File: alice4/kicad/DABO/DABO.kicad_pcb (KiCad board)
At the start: 2 copper layers, 4 parts, among them P1 CONN_01X20, P2 CONN_01X20, P3 CONN_02X20, U1 touchscreen_controller

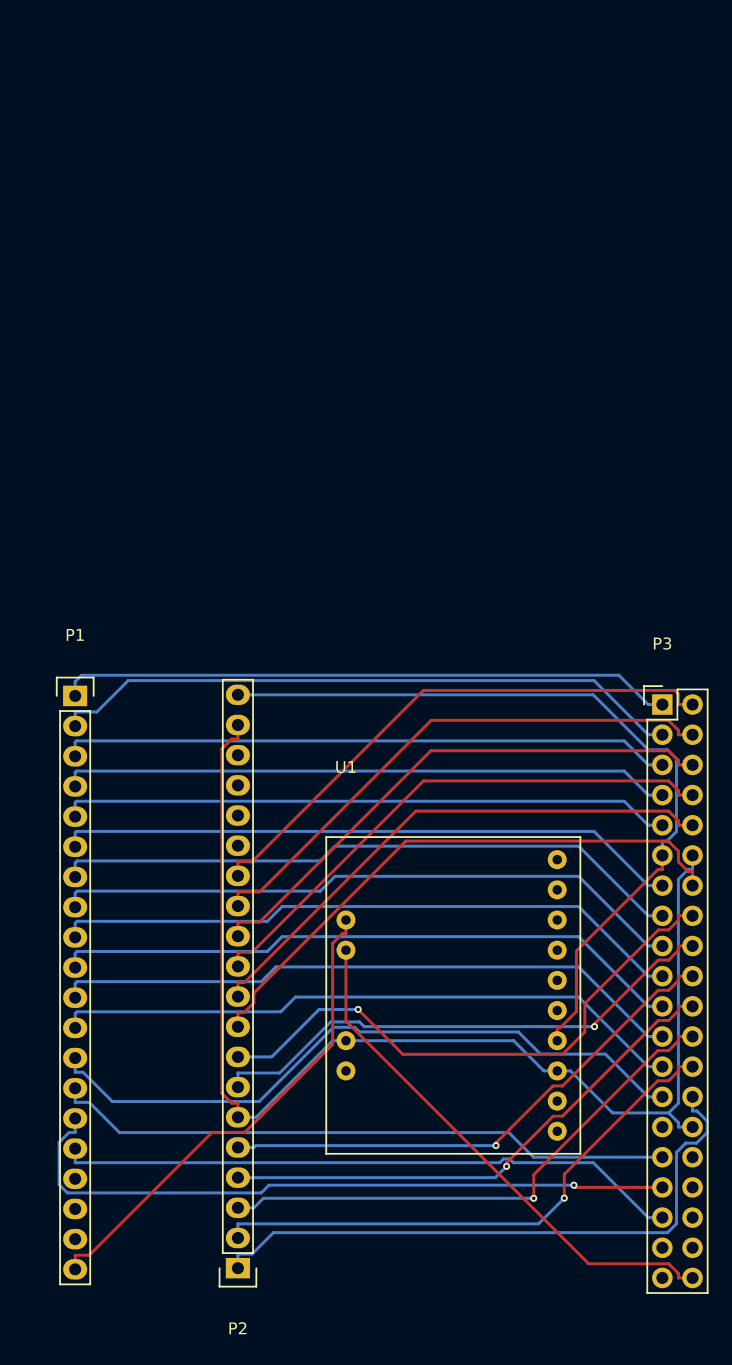
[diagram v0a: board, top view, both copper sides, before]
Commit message: Fix up PCB and footprints further
Fix up number of pads and alignment in STMPE610

Move parts around for better board usage

Move parts around for cable placement
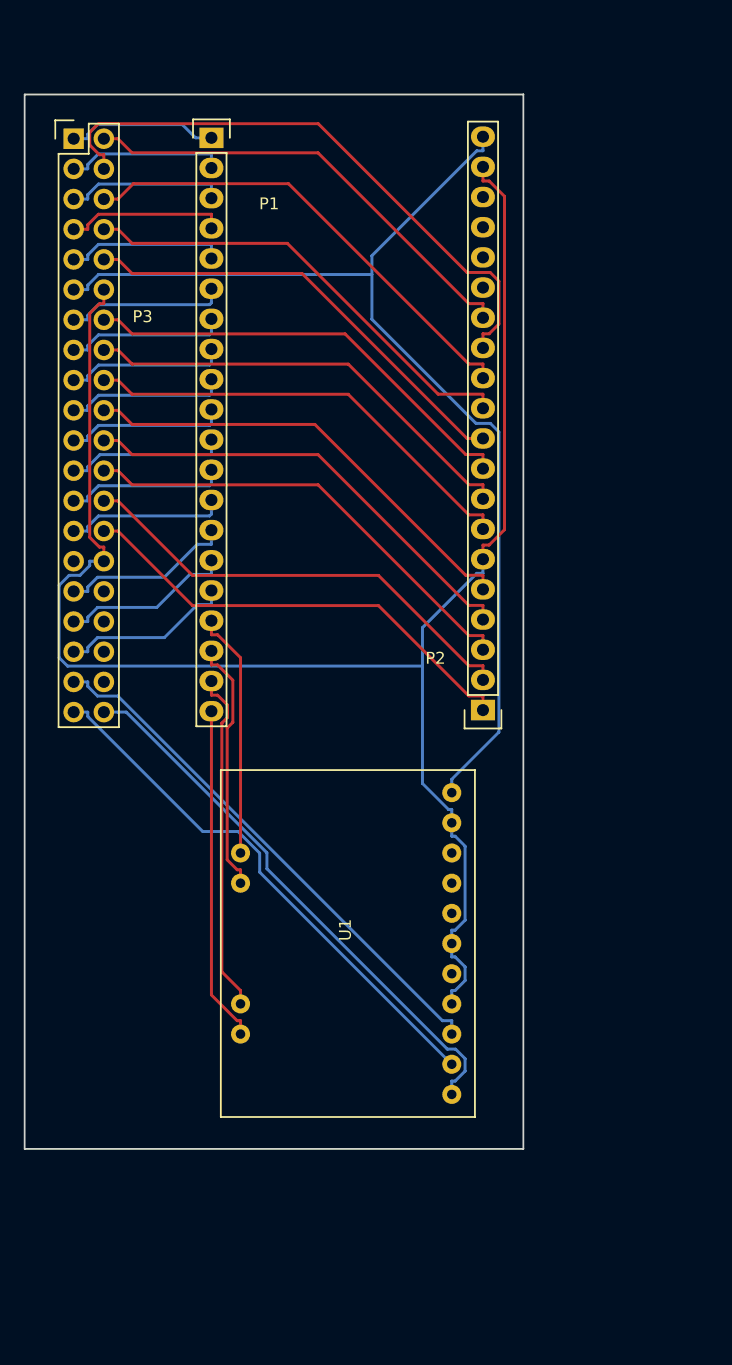
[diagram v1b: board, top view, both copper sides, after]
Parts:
- moved P3 68.7 mm to (135.7, 58.4)
- moved P2 51.3 mm to (170.2, 106.5)
- moved P1 48.4 mm to (147.3, 58.3)
- moved U1 10.5 mm to (149.7, 110.9)
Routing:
- net SCL: track 0.00 -> 45.3 mm
- net INT: track 0.00 -> 45.0 mm
- net B6: track 57.8 -> 14.6 mm, vias 1 -> 0
- net GND: track 101.6 -> 144.7 mm
- net B4: track 56.6 -> 13.6 mm
- net R1: track 53.6 -> 13.5 mm
- net B2: track 53.6 -> 13.6 mm
- net B3: track 53.6 -> 13.6 mm
- net B1: track 53.6 -> 13.6 mm
- net R7: track 53.6 -> 13.6 mm
- net B0: track 53.6 -> 13.6 mm
- net R6: track 53.6 -> 13.6 mm
- net R0: track 51.9 -> 12.8 mm
- net R5: track 52.5 -> 13.6 mm
- net B7: track 52.8 -> 14.6 mm
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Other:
- board outline added: 42 x 88.8 mm

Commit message: Rename SMPTE to STMPE
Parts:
- U1: footprint SMPTE610:Adafruit_SMPTE610 -> STMPE610:Adafruit_STMPE610
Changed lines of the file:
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@@
     (add_net Y-)
   )
-  (module SMPTE610:Adafruit_SMPTE610 (layer F.Cu)
+  (module STMPE610:Adafruit_STMPE610 (layer F.Cu)
     (at 149.745 110.9)
-    (descr "Adafruit SMPTE610 breakout")
+    (descr "Adafruit STMPE610 breakout")
     (tags "dil dip 2.54 400")
     (fp_text reference U1 (at 8.82 14.09 90) (layer F.SilkS)

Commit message: Add 2x7 pin LTC header
Add DIH 14-pin footprint and add to schematic and route
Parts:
- added P4: CONN_02X07, DIH_2x7x2mm:DIH_2x7x2mm, F.Cu at (137.0, 124.2)
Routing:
- net GND: track 144.7 -> 184.8 mm
- net SDA: track 46.9 -> 63.3 mm
- net SCL: track 45.3 -> 54.4 mm
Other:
- board text added: "Alice 4 Daughterboard v1 Brad Grantham March 2017"

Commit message: Add markings to orient LCD board
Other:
- board text added: "5VIN"
- board text added: "R0"
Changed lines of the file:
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@@
     (area 131.499731 54.599999 173.625001 143.500015)
     (thickness 1.6)
-    (drawings 5)
+    (drawings 7)
     (tracks 309)
     (zones 0)
@@
     (descr "Through hole pin header")
     (tags "pin header")
-    (fp_text reference P1 (at 4.8543 5.55) (layer F.SilkS)
+    (fp_text reference P1 (at 4.829 5.375) (layer F.SilkS)
       (effects (font (size 1 1) (thickness 0.15)))
     )
@@
       (net 54 "Net-(P4-Pad2)"))
   )
+  (gr_text 5VIN (at 165.25 58.05) (layer F.SilkS)
+    (effects (font (size 1.5 1.5) (thickness 0.3)))
+  )
+  (gr_text "R0\n" (at 143.925 58.3) (layer F.SilkS)
+    (effects (font (size 1.5 1.5) (thickness 0.3)))
+  )
   (gr_text "Alice 4 Daughterboard v1\nBrad Grantham\nMarch 2017" (at 144.1 125.25 90) (layer F.SilkS)

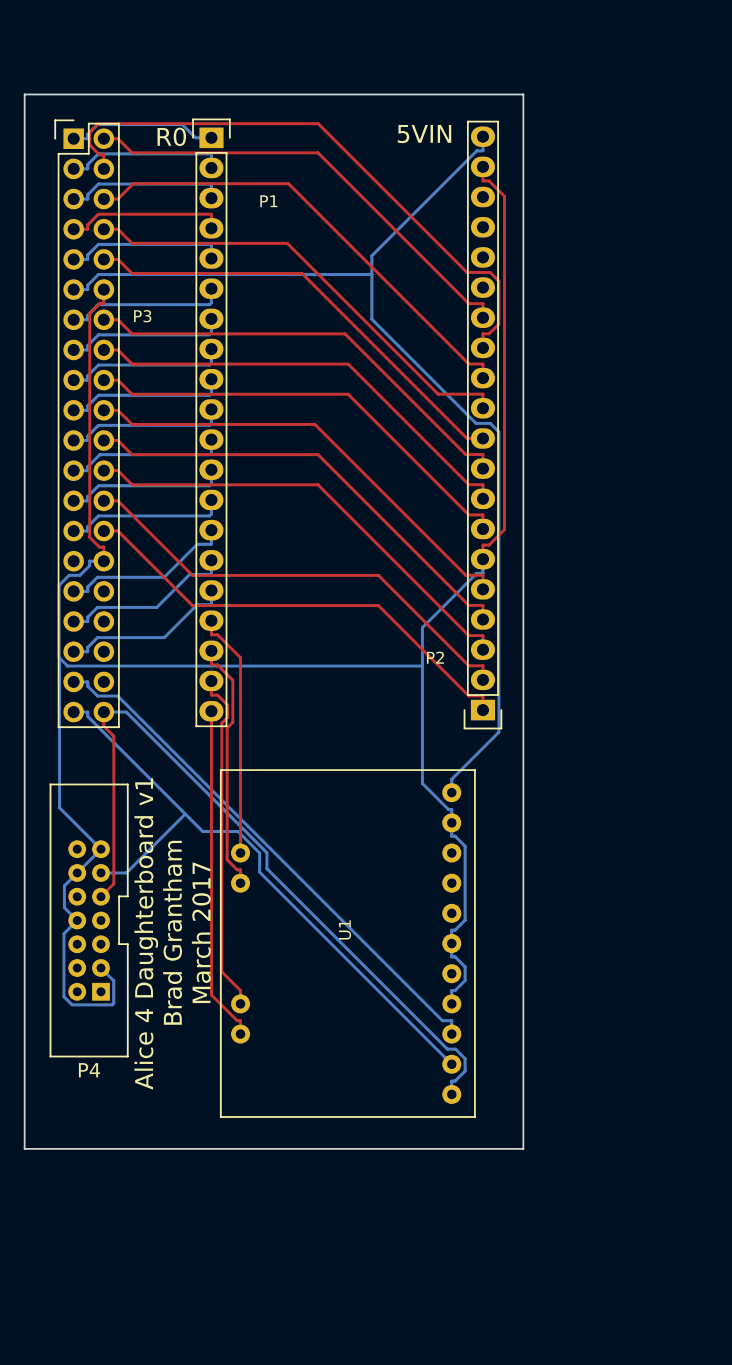
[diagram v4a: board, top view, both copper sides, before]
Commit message: Fix some of Lawrence's issues
Fix X+X- ordering on touchscreen board

Route to correct XL/XR on LCD breakout

LCD, not VGA

Tag power lines with PWR flag

Route pin 27 to backlight PWM on LCD breakout
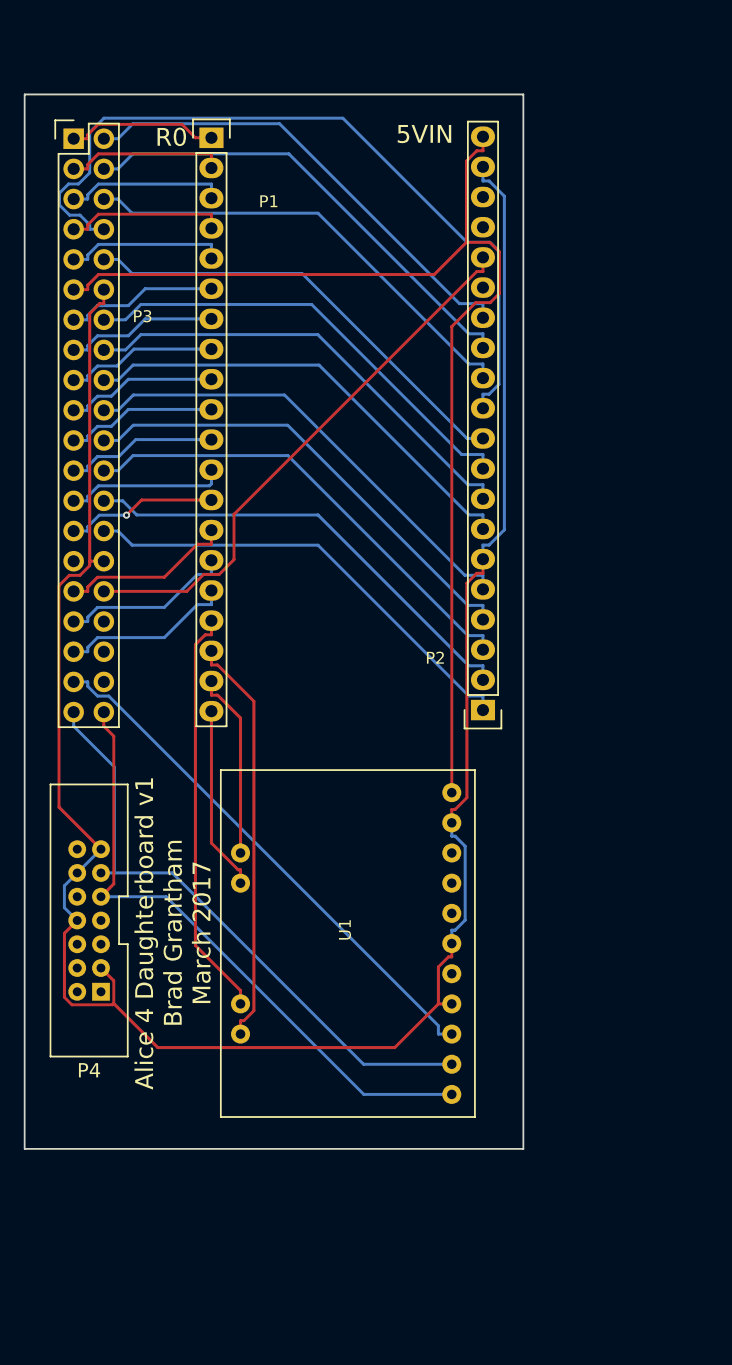
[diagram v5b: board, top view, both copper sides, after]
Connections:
- net VGA_CLK renamed LCD_CLK
- P1 pad 17: X+ -> X-
- P1 pad 19: X- -> X+
- P2 pad 16: Net-(P2-Pad16) -> BACKLIGHT_PWM
- P3 pad 32: Net-(P3-Pad32) -> BACKLIGHT_PWM
- U1 pad 2: Y- -> Y+
- U1 pad 4: Y+ -> Y-
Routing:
- net BACKLIGHT_PWM: track 0.00 -> 46.5 mm
- net G3: track 38.8 -> 66.1 mm
- net Y-: track 21.4 -> 34.7 mm
- net Y+: track 28.4 -> 15.6 mm
- net G1: track 50.5 -> 39.9 mm
- net SDA: track 63.3 -> 52.8 mm
- net X-: track 28.9 -> 34.7 mm
- net X+: track 20.9 -> 15.8 mm
- net +5V: track 92.0 -> 95.7 mm
- net SCL: track 54.4 -> 51.2 mm
- net GND: track 184.8 -> 182.1 mm
- net G2: track 39.9 -> 38.8 mm
- net G6: track 37.8 -> 38.9 mm
- net LCD_CLK: track 38.8 -> 39.9 mm
- net DISPLAY_ON: track 38.8 -> 39.9 mm
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
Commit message: Use better LCD breakout footprint, improve PCB
Add copper pours

Add mounting holes

Use LCD breakout component and footprint
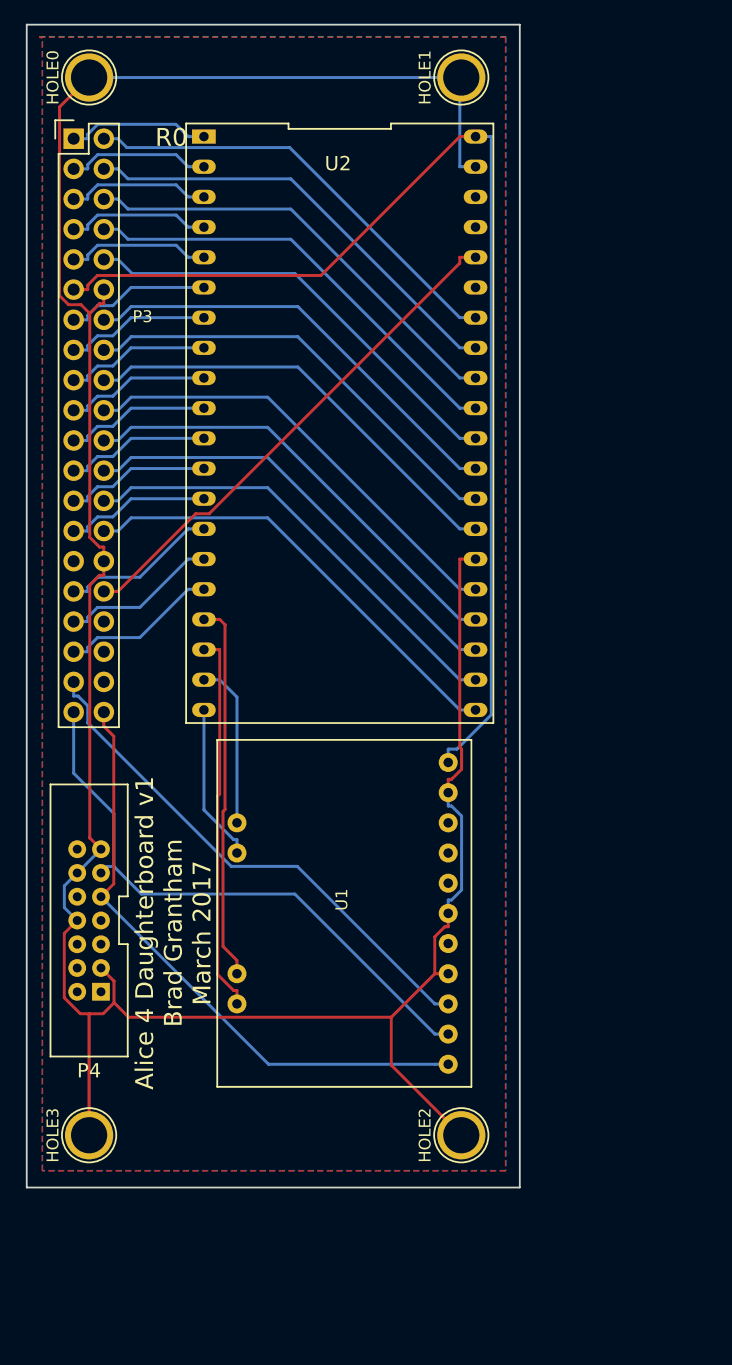
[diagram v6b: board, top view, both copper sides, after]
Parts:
- removed P1, P2: CONN_01X20, Pin_Headers:Pin_Header_Straight_1x20
- added HOLE0: 1pin, Connect:1pin, F.Cu at (137.0, 53.2)
- added HOLE1: 1pin, Connect:1pin, F.Cu at (168.3, 53.2)
- added HOLE2: 1pin, Connect:1pin, F.Cu at (168.3, 142.3)
- added HOLE3: 1pin, Connect:1pin, F.Cu at (137.0, 142.3)
- added U2: LCDBREAKOUT, DIP40:DIP-40_1_ELL, F.Cu at (158.1, 82.3)
- moved U1 2.56 mm to (149.4, 108.4)
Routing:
- net GND: track 182.1 -> 227.1 mm
- net G3: track 66.1 -> 37.5 mm
- net BACKLIGHT_PWM: track 46.5 -> 43.2 mm
- net X-: track 34.7 -> 31.9 mm
- net Y-: track 34.7 -> 32.1 mm
- net G1: track 39.9 -> 37.5 mm
- net G0: track 39.9 -> 37.5 mm
- net Y+: track 15.6 -> 13.4 mm
- net X+: track 15.8 -> 14.0 mm
- net LCD_CLK: track 39.9 -> 38.4 mm
- net DISPLAY_ON: track 39.9 -> 38.4 mm
- net G5: track 38.9 -> 37.4 mm
- net G6: track 38.9 -> 37.4 mm
- net SCL: track 51.2 -> 49.7 mm
- net HSYNC: track 39.9 -> 38.4 mm
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- added copper zone on F.Cu, net +5V
- added copper zone on B.Cu, net GND
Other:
- board size 42 x 88.8 mm -> 41.5 x 97.9 mm
- board text removed: "5VIN"

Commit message: remove pours
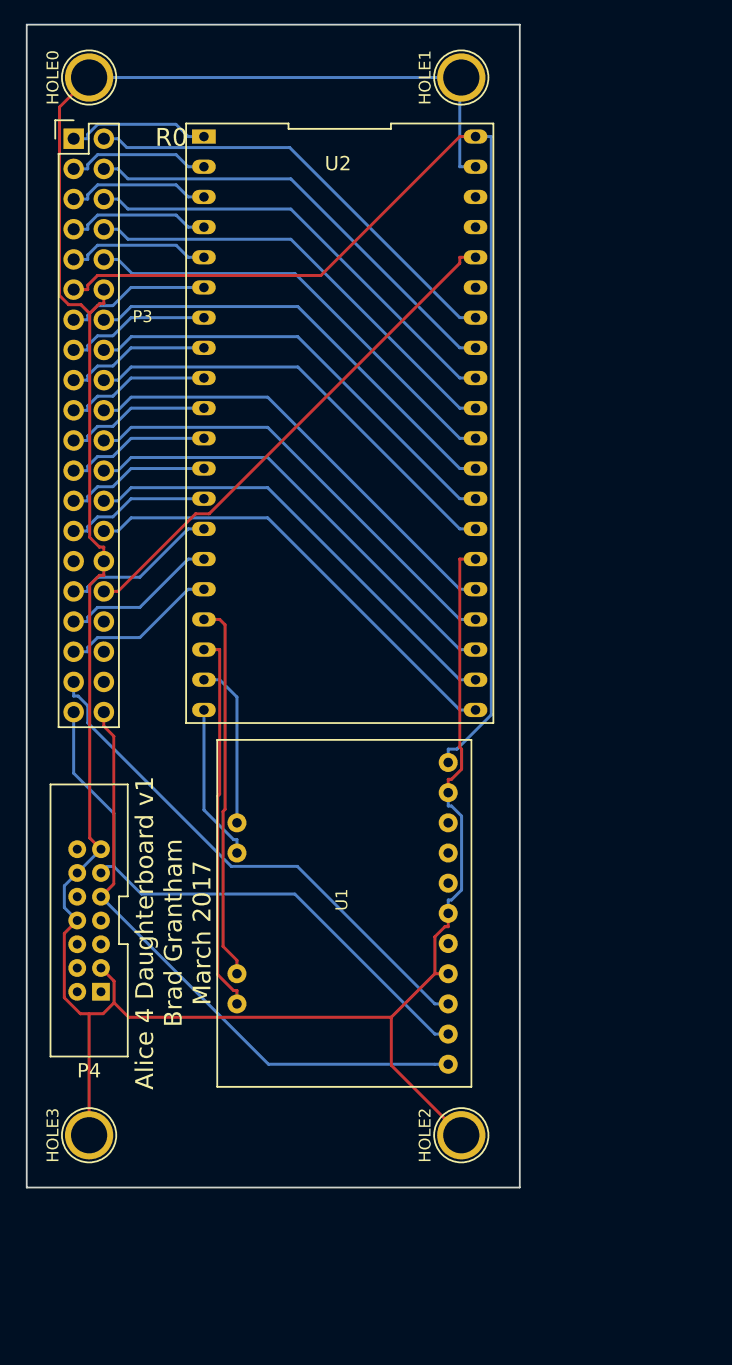
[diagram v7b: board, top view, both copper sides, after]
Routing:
- removed copper zone on F.Cu, net +5V
- removed copper zone on B.Cu, net GND
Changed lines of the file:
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@@
   (segment (start 138.24 96.5) (end 139.4289 96.5) (width 0.25) (layer F.Cu) (net 55))
   (segment (start 169.525 68.38) (end 168.1997 68.38) (width 0.25) (layer F.Cu) (net 55))
-  (zone (net 26) (net_name GND) (layer B.Cu) (hatch edge 0.508)
-    (connect_pads (clearance 0.508))
-    (min_thickness 0.254)
-    (fill yes (arc_segments 16) (thermal_gap 0.508) (thermal_bridge_width 0.508))
-    (polygon
-      (pts
-        (xy 132.825 49.825) (xy 172.075 49.825) (xy 172.075 145.25) (xy 133.075 145.25) (xy 133.075 49.925)
-        (xy 133.025 49.875)
-      )
-    )
-  )
-  (zone (net 35) (net_name +5V) (layer F.Cu) (hatch edge 0.508)
-    (connect_pads (clearance 0.508))
-    (min_thickness 0.254)
-    (fill yes (arc_segments 16) (thermal_gap 0.508) (thermal_bridge_width 0.508))
-    (polygon
-      (pts
-        (xy 132.796282 49.85) (xy 172.046282 49.85) (xy 172.046282 145.275) (xy 133.046282 145.275) (xy 133.046282 49.95)
-        (xy 132.996282 49.9)
-      )
-    )
-  )
 )

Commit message: Handle pours correctly; add zones, then route, then fill
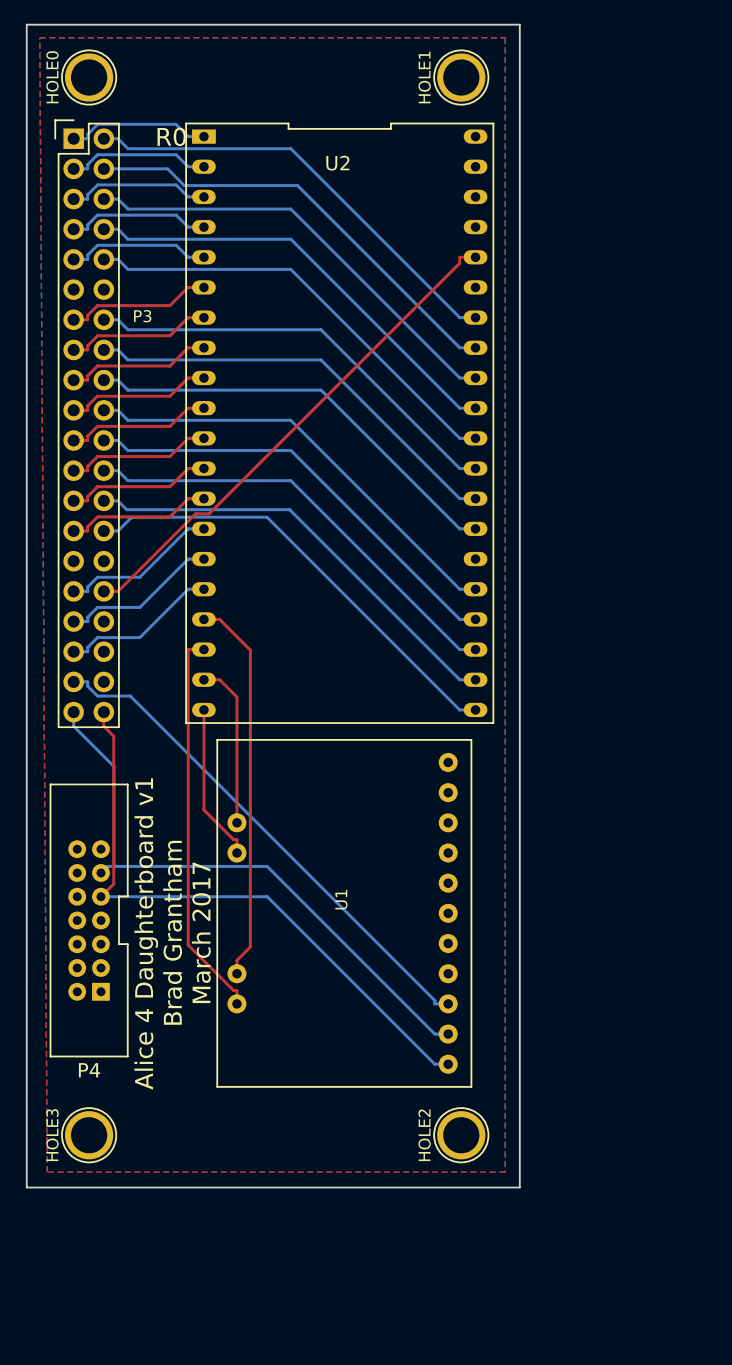
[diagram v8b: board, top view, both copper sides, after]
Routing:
- net GND: track 227.1 -> 0.00 mm
- net +5V: track 95.3 -> 0.00 mm
- net INT: track 44.3 -> 43.1 mm
- net Y-: track 32.1 -> 33.0 mm
- net G6: track 37.4 -> 36.5 mm
- net G5: track 37.4 -> 36.5 mm
- net VSYNC: track 38.4 -> 37.5 mm
- net HSYNC: track 38.4 -> 37.5 mm
- net DISPLAY_ON: track 38.4 -> 37.5 mm
- net LCD_CLK: track 38.4 -> 37.5 mm
- net G7: track 37.4 -> 36.5 mm
- net X-: track 31.9 -> 32.7 mm
- added copper zone on F.Cu, net +5V
- added copper zone on B.Cu, net GND
